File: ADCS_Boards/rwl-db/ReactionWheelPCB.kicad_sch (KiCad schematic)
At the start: 47 parts, among them J1 PC104_Connector, J2 Conn_1, J3 Conn_2, J4 Conn_3, J5 Conn_4, U1 Controller 1, U2 Controller 2, U3 Controller 3, U4 Controller 4, U5 LM358, U6 LM358

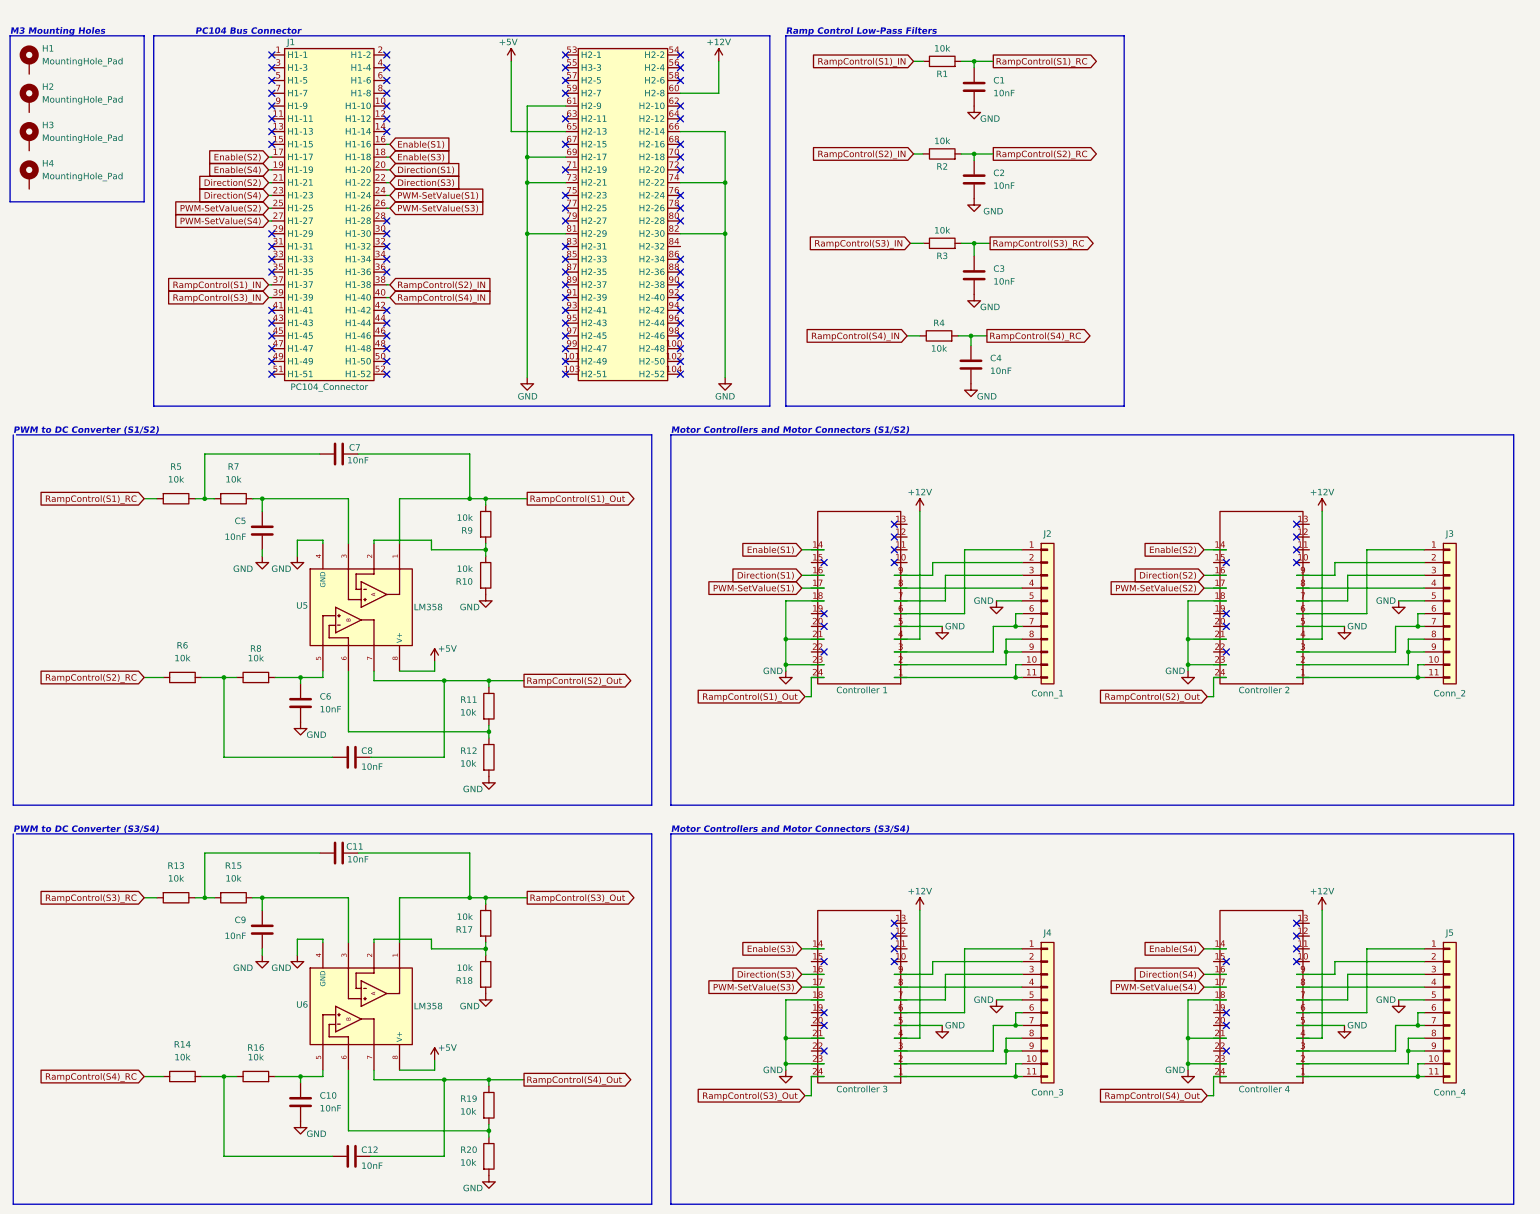
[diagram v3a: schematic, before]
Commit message: adcs: Updated rw-db with latest PWM filter design and added misc silkscreen
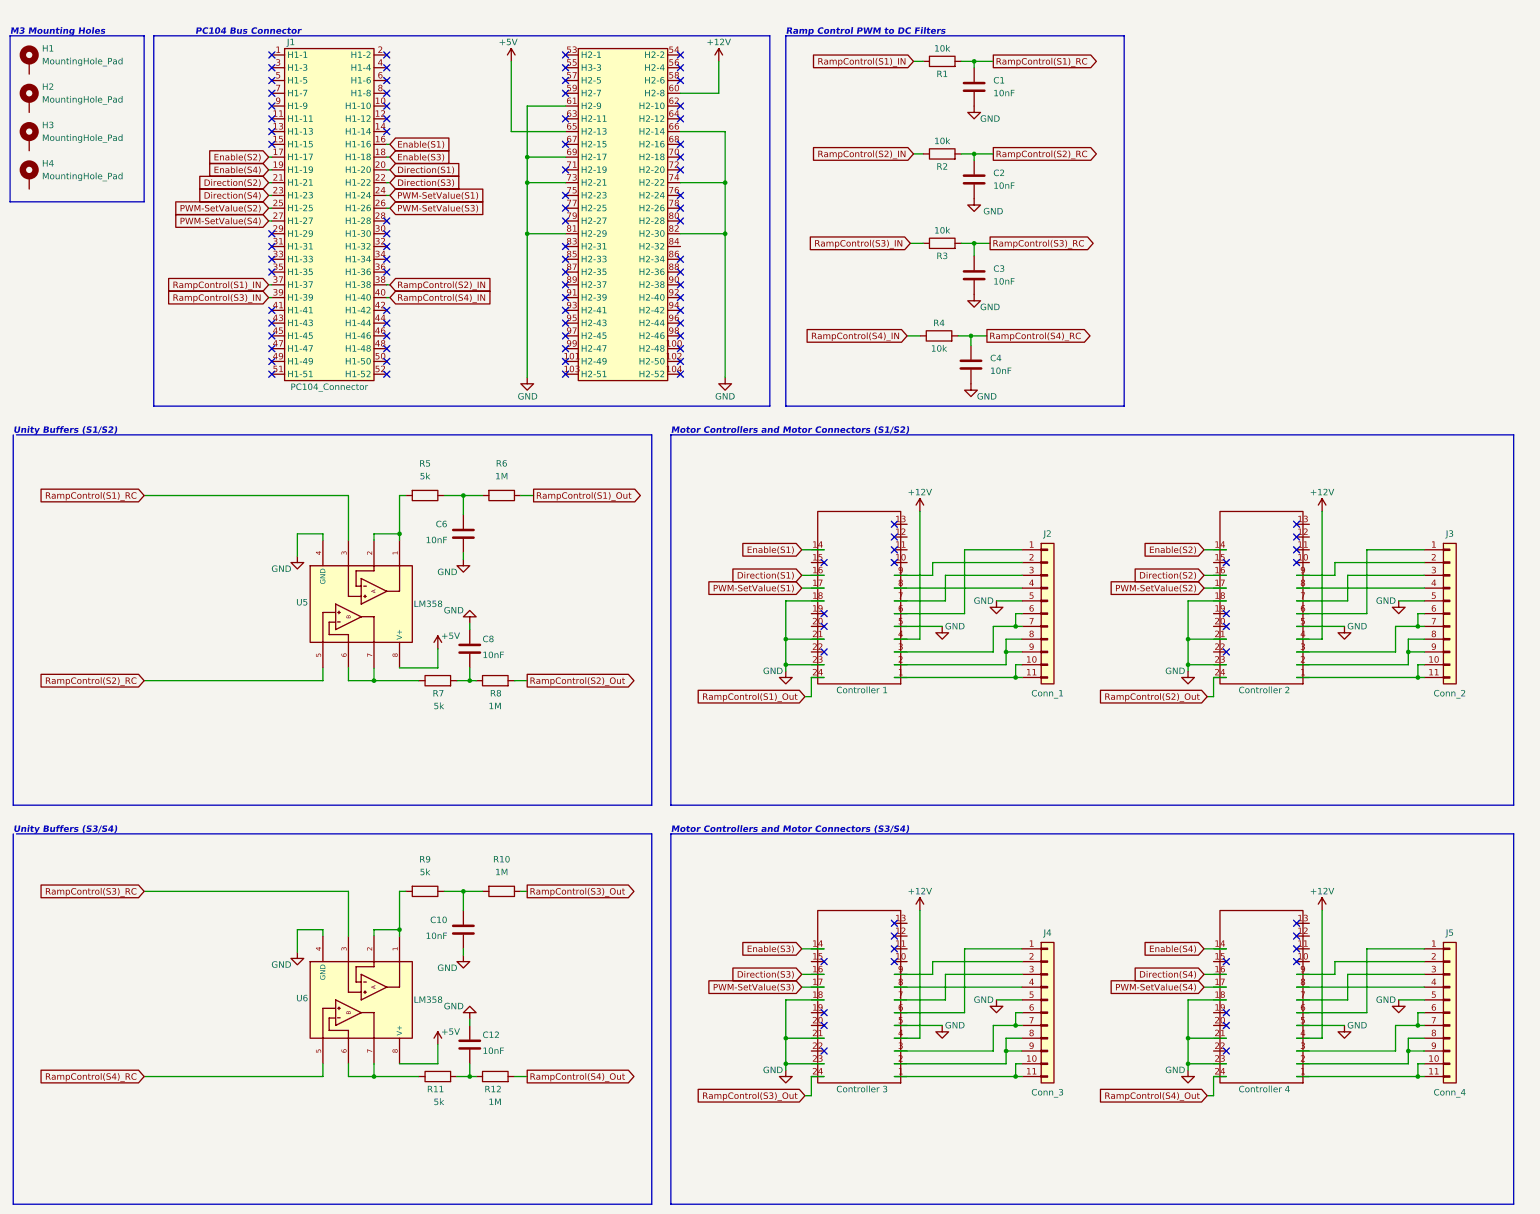
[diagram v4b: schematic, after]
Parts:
- removed C11, C5, C7, C9: 10nF, Capacitor_SMD:C_0603_1608Metric, symbol Device:C
- removed R13, R14, R15, R16, R17, R18, R19, R20, R7: 10k, Resistor_SMD:R_0603_1608Metric, symbol Device:R
- added R11: 5k, Resistor_SMD:R_0603_1608Metric, symbol Device:R
- R10, R12, R6, R8: value 10k -> 1M
- R5, R9: value 10k -> 5k
- R7: renamed from R11; value 10k -> 5k
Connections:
- net GND: now also C10.1, C12.1, C6.1, C8.1; no longer C10.2, C6.2, R10.2, R12.2
- net RampControl(S1)_Out: now also R6.1; no longer R9.1, U5.1
- net RampControl(S1)_RC: now also U5.3; no longer R5.2
- net RampControl(S2)_Out: now also R8.2; no longer C8.1, R7.1, U5.7
- net RampControl(S2)_RC: now also U5.5; no longer R6.1
- net RampControl(S3)_Out: now also R10.1; no longer U6.1
- net RampControl(S3)_RC: now also U6.3
- net RampControl(S4)_Out: now also R12.2; no longer C12.1, U6.7
- net RampControl(S4)_RC: now also U6.5
- net at C12.2: now also R12.1, R11.2
- net at U6.2: now also R9.2, U6.1
- net at C8.2, R8.1: now also R7.2; no longer R6.2
- net at R5.1: now also C6.2, R6.2
- net at U6.6: now also U6.7, R11.1
- new net: R7.1, U5.6, U5.7
- new net: C10.2, R10.2, R9.1
- new net: R5.2, U5.1, U5.2
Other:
- note added: "Ramp Control PWM to DC Filters"
- note added: "Unity Buffers (S1/S2)"
- note added: "Unity Buffers (S3/S4)"
- note removed: "PWM to DC Converter (S1/S2)"
- note removed: "PWM to DC Converter (S3/S4)"
- note removed: "Ramp Control Low-Pass Filters"
- moved on the sheet: C8, R7, U5, U6

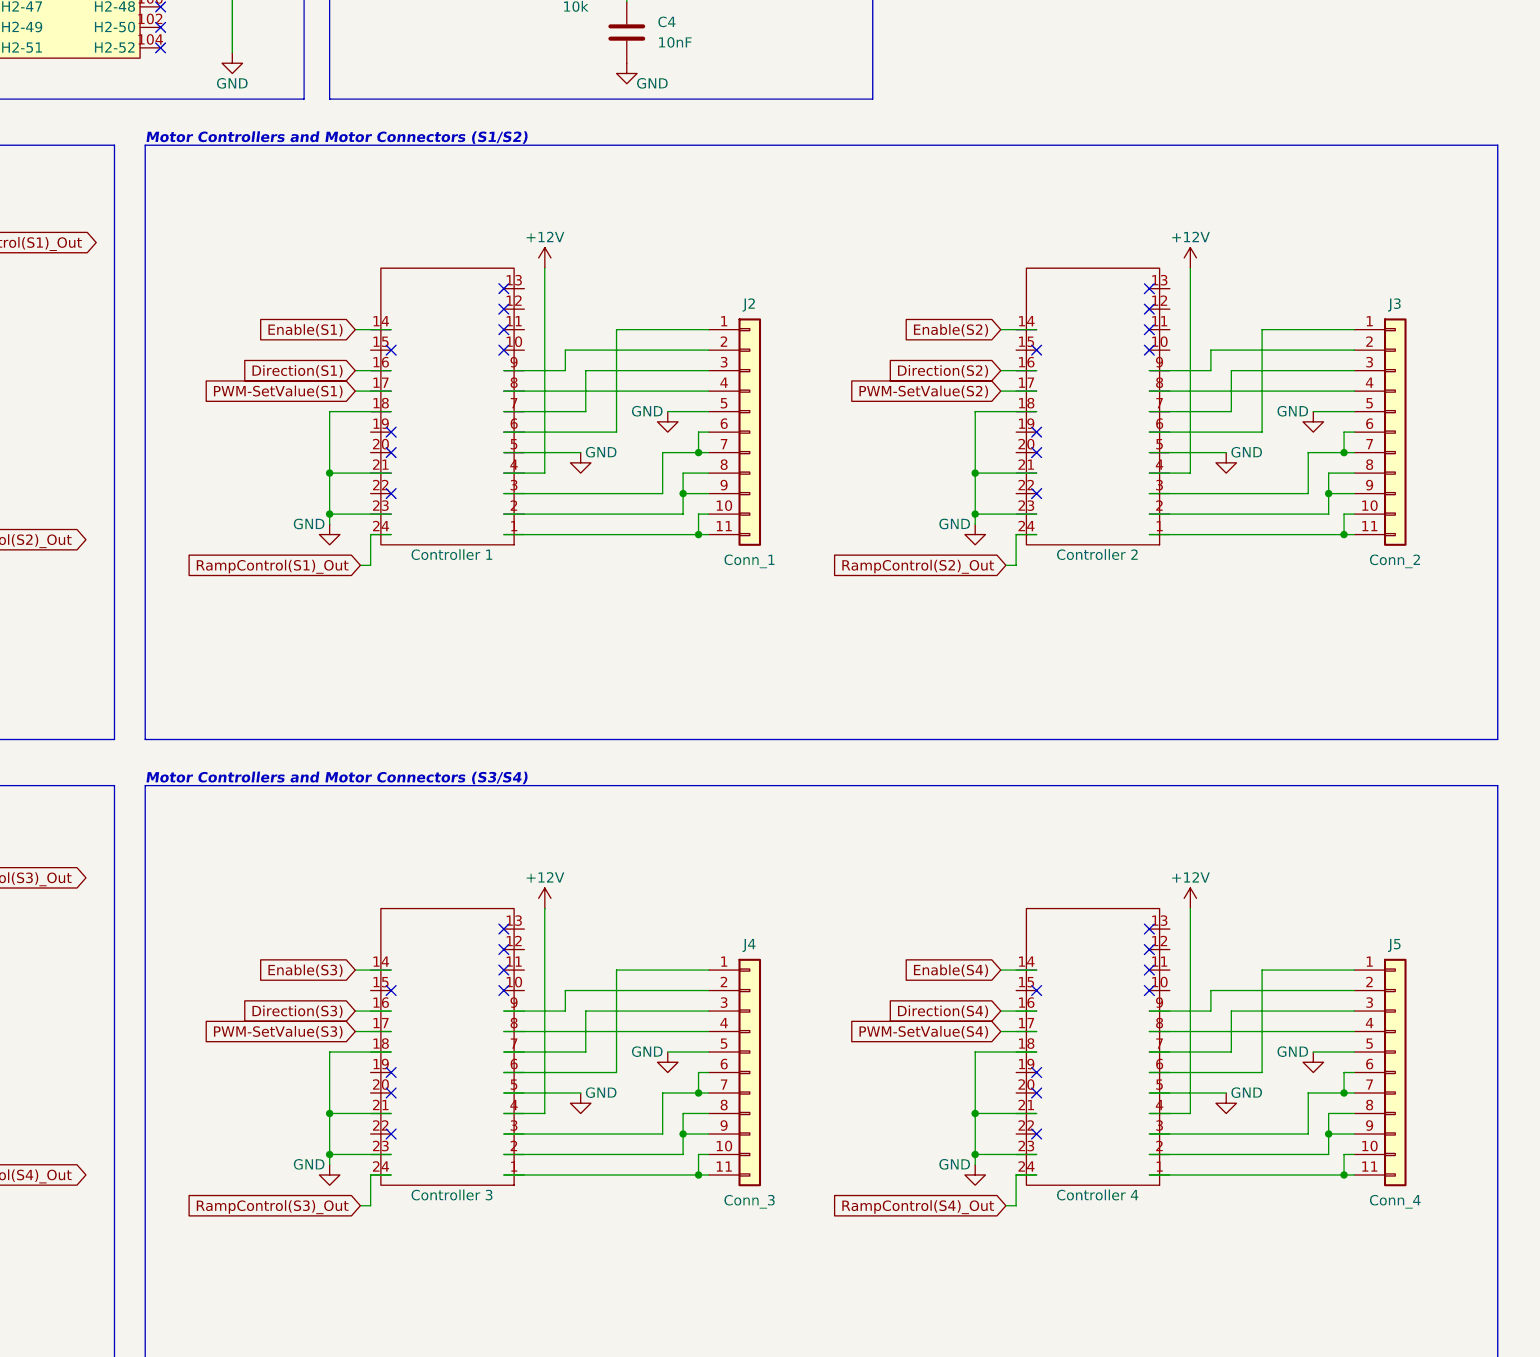
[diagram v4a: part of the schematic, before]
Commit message: adcs: rwl-db: change rwl connector to vertical type
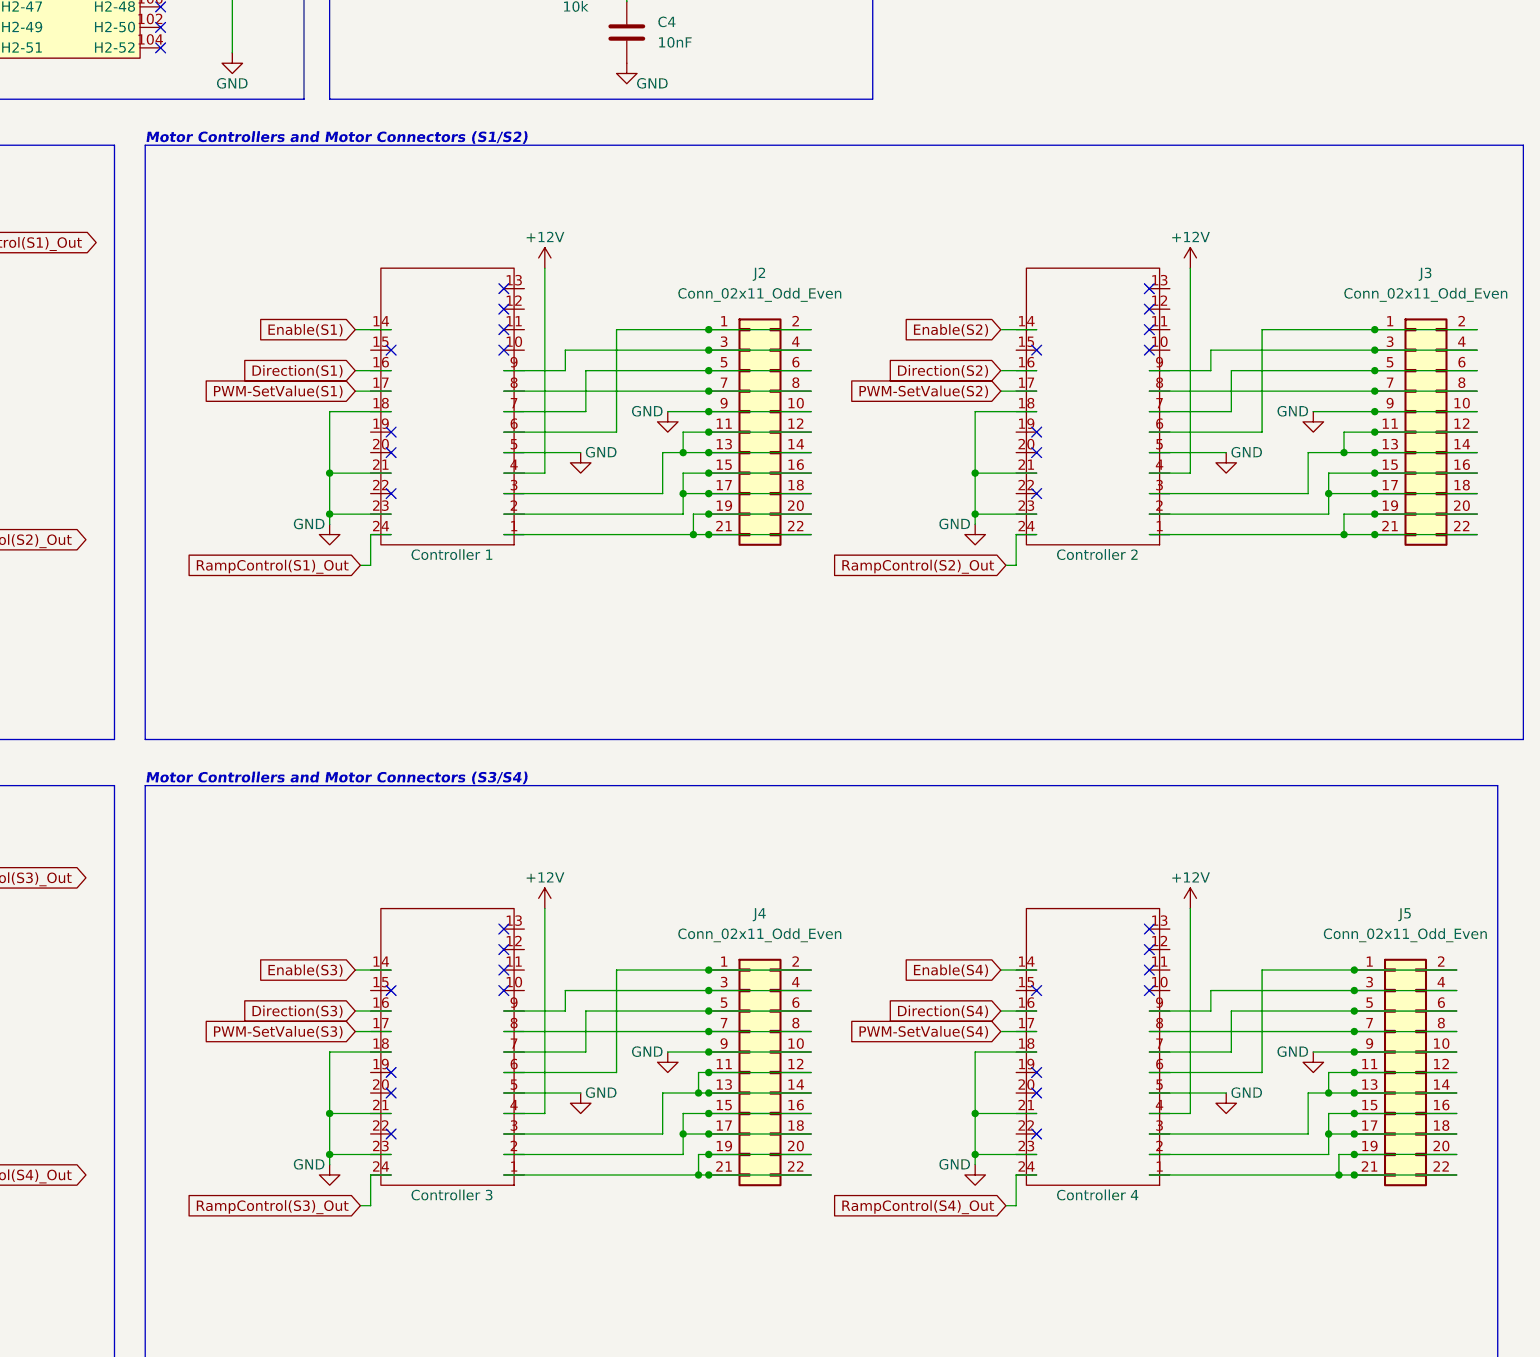
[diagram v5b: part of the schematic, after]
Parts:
- removed J2: Conn_1, qset-footprints:FPC_11_SAT_1-84953-1, symbol Connector_Generic:Conn_01x11
- removed J3: Conn_2, qset-footprints:FPC_11_SAT_1-84953-1, symbol Connector_Generic:Conn_01x11
- removed J4: Conn_3, qset-footprints:FPC_11_SAT_1-84953-1, symbol Connector_Generic:Conn_01x11
- removed J5: Conn_4, qset-footprints:FPC_11_SAT_1-84953-1, symbol Connector_Generic:Conn_01x11
- added J2, J3, J4, J5: Conn_02x11_Odd_Even, qset-footprints:1-1734248-1-reaction-wheel-connector, symbol Connector_Generic:Conn_02x11_Odd_Even
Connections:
- net GND: now also J2.10 (Pin_10), J2.9 (Pin_9), J3.10 (Pin_10), J3.9 (Pin_9), J4.10 (Pin_10), J4.9 (Pin_9), J5.10 (Pin_10), J5.9 (Pin_9)
- net at U3.6: now also J4.1 (Pin_1), J4.2 (Pin_2)
- net at U3.1: now also J4.19 (Pin_19), J4.20 (Pin_20), J4.21 (Pin_21), J4.22 (Pin_22)
- net at U3.9: now also J4.3 (Pin_3), J4.4 (Pin_4)
- net at U3.7: now also J4.5 (Pin_5), J4.6 (Pin_6)
- net at U3.8: now also J4.7 (Pin_7), J4.8 (Pin_8)
- net at U3.3: now also J4.11 (Pin_11), J4.12 (Pin_12), J4.13 (Pin_13), J4.14 (Pin_14)
- net at U3.2: now also J4.15 (Pin_15), J4.16 (Pin_16), J4.17 (Pin_17), J4.18 (Pin_18)
- net at U4.6: now also J5.1 (Pin_1), J5.2 (Pin_2)
- net at U4.1: now also J5.19 (Pin_19), J5.20 (Pin_20), J5.21 (Pin_21), J5.22 (Pin_22)
- net at U4.9: now also J5.3 (Pin_3), J5.4 (Pin_4)
- net at U4.7: now also J5.5 (Pin_5), J5.6 (Pin_6)
- net at U4.8: now also J5.7 (Pin_7), J5.8 (Pin_8)
- net at U4.3: now also J5.11 (Pin_11), J5.12 (Pin_12), J5.13 (Pin_13), J5.14 (Pin_14)
- net at U4.2: now also J5.15 (Pin_15), J5.16 (Pin_16), J5.17 (Pin_17), J5.18 (Pin_18)
- net at U2.6: now also J3.1 (Pin_1), J3.2 (Pin_2)
- net at U2.1: now also J3.19 (Pin_19), J3.20 (Pin_20), J3.21 (Pin_21), J3.22 (Pin_22)
- net at U2.9: now also J3.3 (Pin_3), J3.4 (Pin_4)
- net at U2.7: now also J3.5 (Pin_5), J3.6 (Pin_6)
- net at U2.8: now also J3.7 (Pin_7), J3.8 (Pin_8)
- net at U2.3: now also J3.11 (Pin_11), J3.12 (Pin_12), J3.13 (Pin_13), J3.14 (Pin_14)
- net at U2.2: now also J3.15 (Pin_15), J3.16 (Pin_16), J3.17 (Pin_17), J3.18 (Pin_18)
- net at U1.6: now also J2.1 (Pin_1), J2.2 (Pin_2)
- net at U1.1: now also J2.19 (Pin_19), J2.20 (Pin_20), J2.21 (Pin_21), J2.22 (Pin_22)
- net at U1.9: now also J2.3 (Pin_3), J2.4 (Pin_4)
- net at U1.7: now also J2.5 (Pin_5), J2.6 (Pin_6)
- net at U1.8: now also J2.7 (Pin_7), J2.8 (Pin_8)
- net at U1.3: now also J2.11 (Pin_11), J2.12 (Pin_12), J2.13 (Pin_13), J2.14 (Pin_14)
- net at U1.2: now also J2.15 (Pin_15), J2.16 (Pin_16), J2.17 (Pin_17), J2.18 (Pin_18)
